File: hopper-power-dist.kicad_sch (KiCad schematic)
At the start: 30 parts, among them J1 XT90PW-M, J2 B2B-XH-A(LF)(SN), J3 XT60PW-F, J4 XT60PW-F, J5 XT60PW-F, J6 XT60PW-F, J7 XT60PW-F, J8 B2B-XH-A(LF)(SN), SW2 FT_Power_Switch

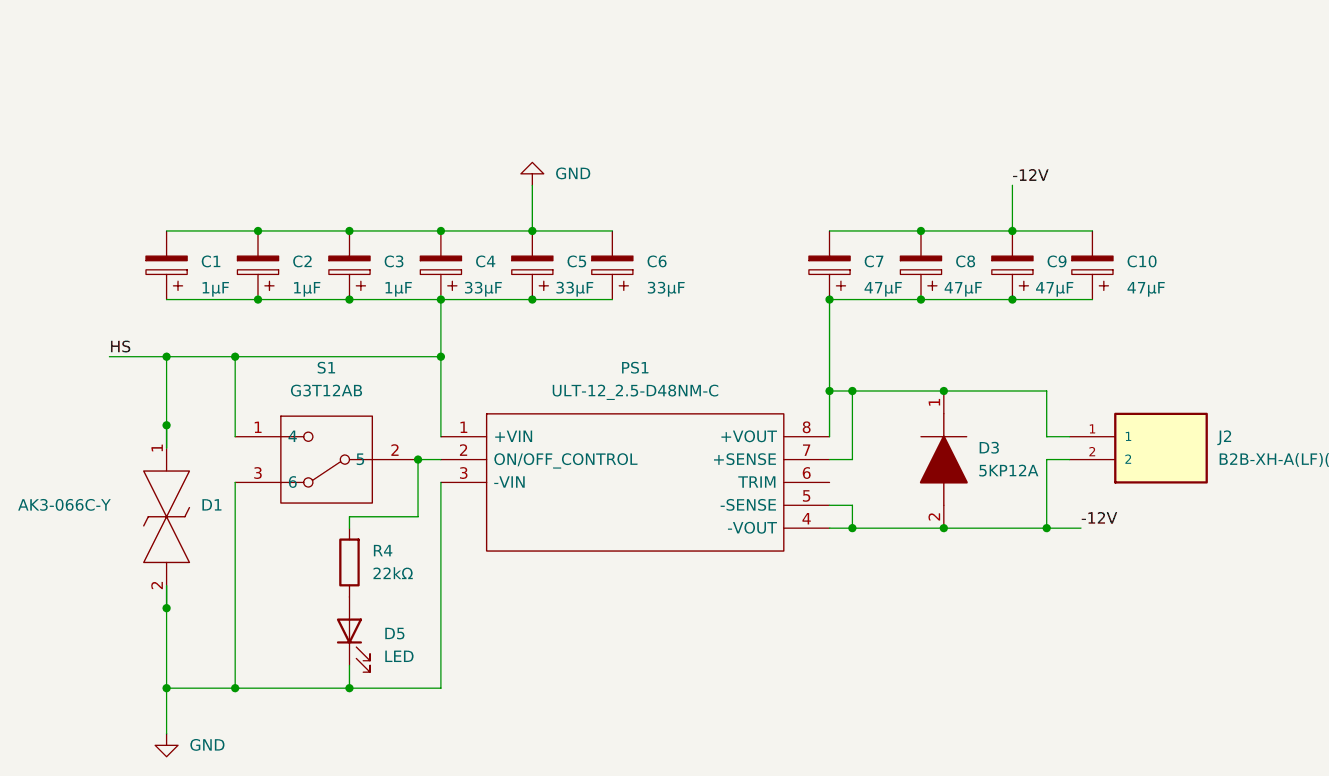
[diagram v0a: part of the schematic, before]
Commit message: Fix schematic and update 3d models
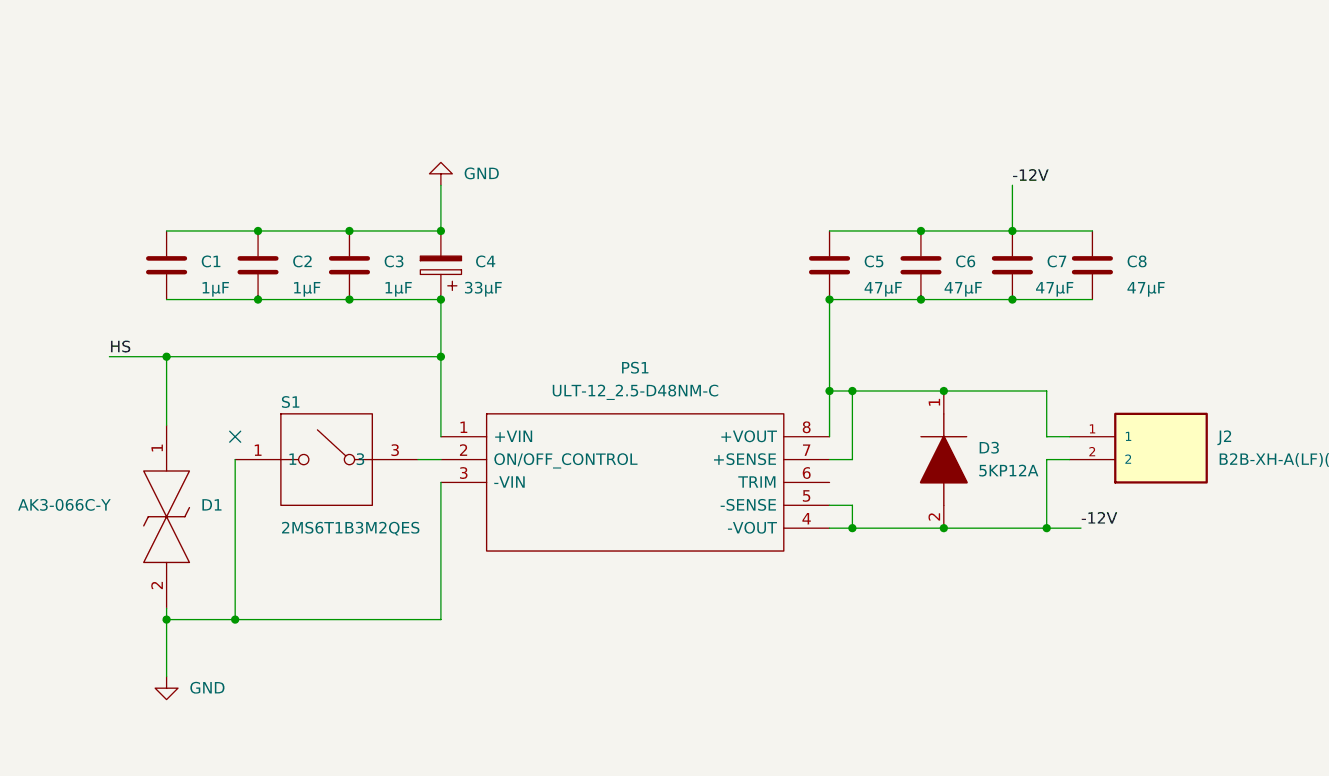
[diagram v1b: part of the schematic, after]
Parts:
- removed C5, C6: 33μF, Capacitor_SMD:CP_Elec_8x10, symbol Device:C_Polarized
- removed D5: LED, LED_SMD:LED_0603_1608Metric, symbol Device:LED
- removed R4: 22kΩ, Resistor_SMD:R_0603_1608Metric_Pad0.98x0.95mm_HandSolder, symbol Device:R
- removed S1: G3T12AB, G3T12AB, symbol SamacSys_Parts:G3T12AB
- added S1: 2MS6T1B3M2QES, 2MS6T1B3M2QES, symbol benbokser:2MS6T1B3M2QES
- C1, C2, C3: footprint Capacitor_SMD:CP_Elec_8x10 -> Capacitor_SMD:C_1206_3216Metric; symbol Device:C_Polarized -> Device:C
- C5: renamed from C7; footprint Capacitor_SMD:CP_Elec_8x10 -> Capacitor_SMD:C_2220_5650Metric; symbol Device:C_Polarized -> Device:C
- C6: renamed from C8; footprint Capacitor_SMD:CP_Elec_8x10 -> Capacitor_SMD:C_2220_5650Metric; symbol Device:C_Polarized -> Device:C
- C7: renamed from C9; footprint Capacitor_SMD:CP_Elec_8x10 -> Capacitor_SMD:C_2220_5650Metric; symbol Device:C_Polarized -> Device:C
- C8: renamed from C10; footprint Capacitor_SMD:CP_Elec_8x10 -> Capacitor_SMD:C_2220_5650Metric; symbol Device:C_Polarized -> Device:C
- R2: footprint SamacSys_Parts:RESAD5390W86L2222D792 -> benbokser:CW005900R0JB12
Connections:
- net GND: now also S1.1
- net at PS1.2 (ON/OFF_CONTROL): now also S1.3
- no-connect marks 0 -> 1

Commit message: Changed precharge resistor, routed PCB traces and updated 3D models
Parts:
- D3: footprint SamacSys_Parts:DIOAD4425W136L885D885 -> benbokser:5KP12A
- R2: value 900Ω -> 365Ω; footprint benbokser:CW005900R0JB12 -> benbokser:AC03000003600JAC00
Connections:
- no-connect marks 1 -> 0
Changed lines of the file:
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@@
   (junction (at 69.85 119.38) (diameter 0) (color 0 0 0 0)
   )
-  (no_connect (at 46.99 134.62))
   (wire (pts (xy 133.35 106.68) (xy 133.35 111.76))
     (stroke (width 0) (type default) (color 0 0 0 0))
@@
       (effects (font (size 1.27 1.27)) (justify left))
     )
-    (property "Footprint" "SamacSys_Parts:DIOAD4425W136L885D885" (id 2) (at 125.73 140.97 0)
+    (property "Footprint" "benbokser:5KP12A" (id 2) (at 125.73 140.97 0)
       (effects (font (size 1.27 1.27)) (justify left) hide)
     )
@@
     (in_bom yes) (on_board yes) (fields_autoplaced)
     (property "Reference" "R2" (id 0) (at 84.455 50.8 90))
-    (property "Value" "900Ω" (id 1) (at 84.455 53.34 90))
-    (property "Footprint" "benbokser:CW005900R0JB12" (id 2) (at 84.455 58.928 90)
+    (property "Value" "365Ω" (id 1) (at 84.455 53.34 90))
+    (property "Footprint" "benbokser:AC03000003600JAC00" (id 2) (at 84.455 58.928 90)
       (effects (font (size 1.27 1.27)) hide)
     )
@@
     )
     (path "/6d558682-e19a-4c65-b77e-d608f0f3e1f5"
-      (reference "D3") (unit 1) (value "5KP12A") (footprint "SamacSys_Parts:DIOAD4425W136L885D885")
+      (reference "D3") (unit 1) (value "5KP12A") (footprint "benbokser:5KP12A")
     )
     (path "/612105e5-ac66-49d2-a8fd-540e901763e8"
@@
     )
     (path "/c5098257-5571-47c3-a82b-49312500a93f"
-      (reference "R2") (unit 1) (value "900Ω") (footprint "benbokser:CW005900R0JB12")
+      (reference "R2") (unit 1) (value "365Ω") (footprint "benbokser:AC03000003600JAC00")
     )
     (path "/d9f35c5b-7a24-4156-809c-cf432f477e68"

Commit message: Start rev02, fix minor mistakes and add xt60pw-m series
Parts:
- removed D2: LED, LED_SMD:LED_0603_1608Metric, symbol Device:LED
- removed J1: XT90PW-M, XT90PW-M:AMASS_XT90PW-M, symbol XT90PW-M:XT90PW-M
- removed R1: 22kΩ, Resistor_SMD:R_0603_1608Metric_Pad0.98x0.95mm_HandSolder, symbol Device:R
- added H1: B-, MountingHole:MountingHole_4.3mm_M4_Pad_Via, symbol Mechanical:MountingHole_Pad
- added H2: C-, MountingHole:MountingHole_4.3mm_M4_Pad_Via, symbol Mechanical:MountingHole_Pad
- added J1, J2: XT60PW-M, XT60PW-F:AMASS_XT60PW-M, symbol XT60PW-F:XT60PW-M
- C4: footprint Capacitor_SMD:CP_Elec_8x10 -> benbokser:CP_Elec_8x10_MAL214699903E3
- D1: footprint SamacSys_Parts:AK3066CY -> AK3066CY
- J3: renamed from J8; footprint B2B-XH-A_LF__SN_:JST_B2B-XH-A(LF)(SN) -> JST_B2B-XH-A(LF)(SN)
- J4: renamed from J2; footprint B2B-XH-A_LF__SN_:JST_B2B-XH-A(LF)(SN) -> JST_B2B-XH-A(LF)(SN)
- J5: renamed from J3; footprint XT60PW-F:AMASS_XT60PW-F -> AMASS_XT60PW-F
- J6: renamed from J4; footprint XT60PW-F:AMASS_XT60PW-F -> AMASS_XT60PW-F
- J7: renamed from J5; footprint XT60PW-F:AMASS_XT60PW-F -> AMASS_XT60PW-F
- J8: renamed from J6; footprint XT60PW-F:AMASS_XT60PW-F -> AMASS_XT60PW-F
- J9: renamed from J7; footprint XT60PW-F:AMASS_XT60PW-F -> AMASS_XT60PW-F
- PS1: footprint SamacSys_Parts:ULT1225D48NMC -> ULT1225D48NMC
- renumbered D3 to D2, D4 to D3, R2 to R1, R3 to R2, SW2 to SW1
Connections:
- net GND: now also H2.1; no longer J5.S1 (SHIELD), J5.S2 (SHIELD), J6.S1 (SHIELD), J6.S2 (SHIELD), J7.S1 (SHIELD), J7.S2 (SHIELD), J8.S1 (SHIELD), J8.S2 (SHIELD), J9.S1 (SHIELD), J9.S2 (SHIELD)
- net at J3.2, SW1.1: now also J2.1 (+)
- new net: J1.1 (+), J2.2 (-)
- new net: H1.1, J1.2 (-)
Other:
- moved on the sheet: J3, R1, SW1

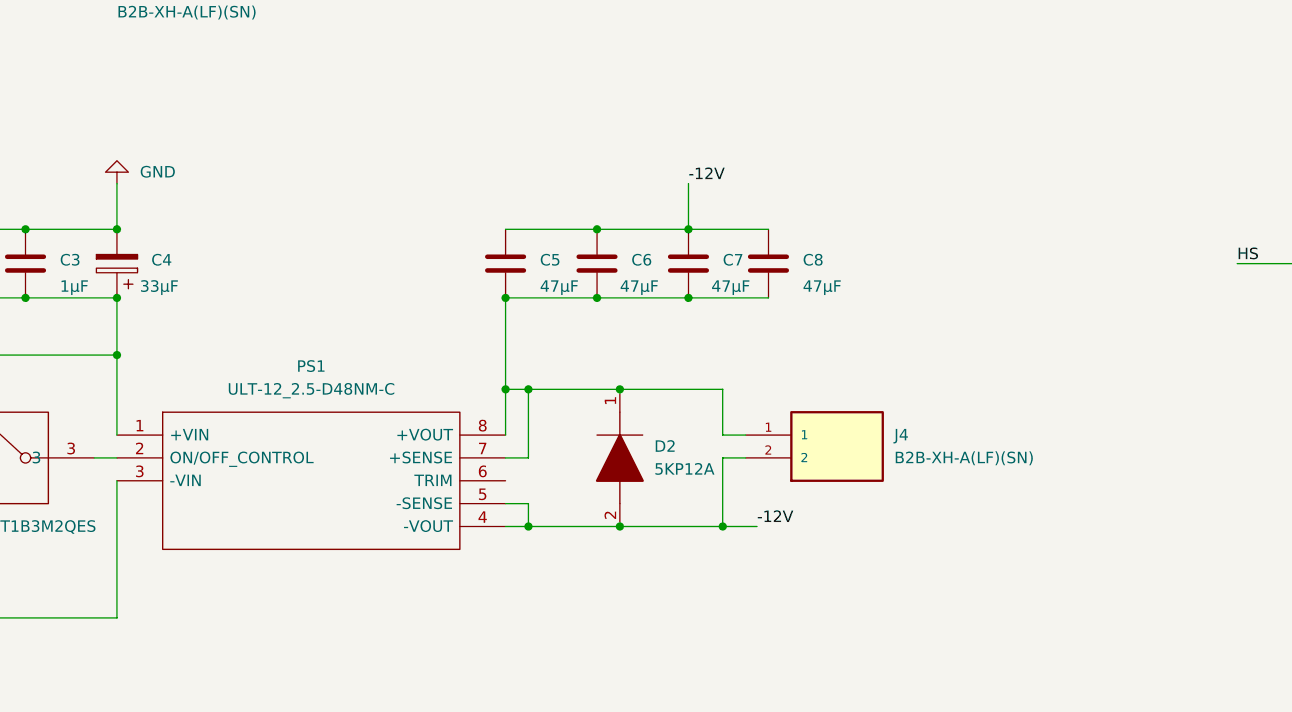
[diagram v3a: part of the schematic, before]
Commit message: Replace DC-DC converter with thru-hole version and clean up
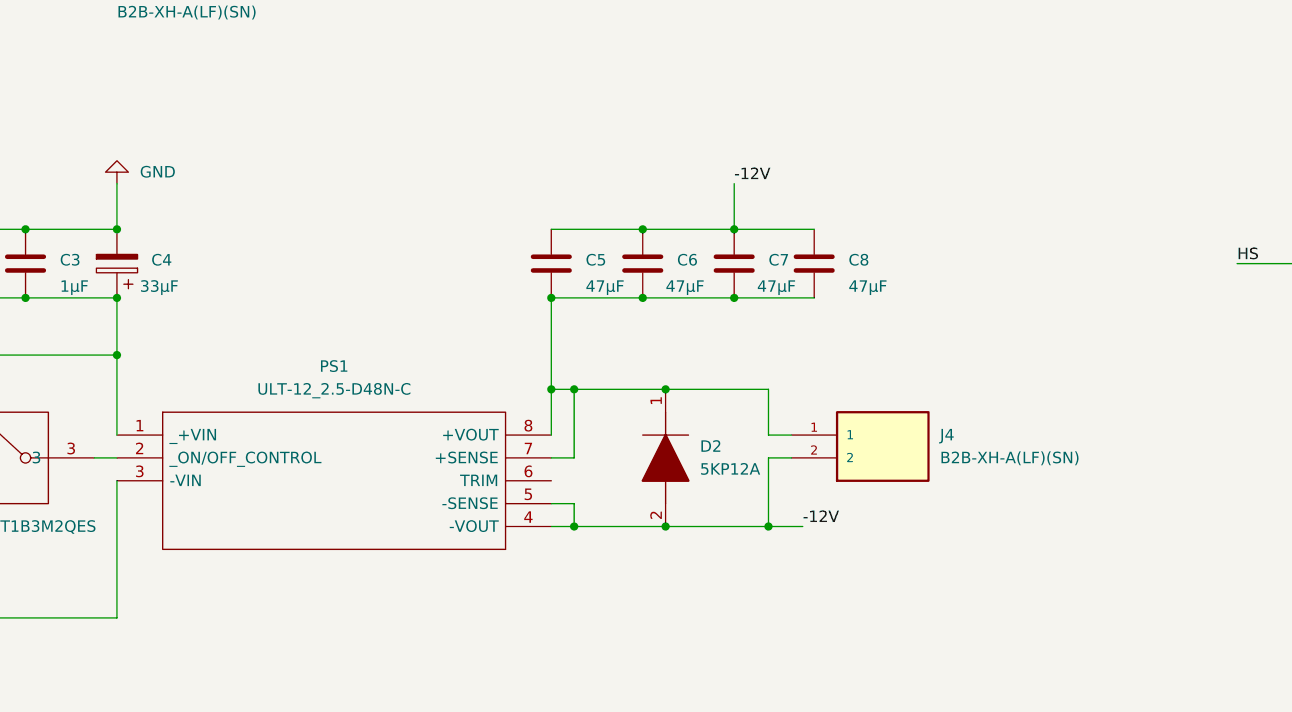
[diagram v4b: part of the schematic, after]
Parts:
- PS1: value ULT-12_2.5-D48NM-C -> ULT-12_2.5-D48N-C; footprint ULT1225D48NMC -> SamacSys_Parts:ULT1225D48NC; symbol SamacSys_Parts:ULT-12_2.5-D48NM-C -> SamacSys_Parts:ULT-12_2.5-D48N-C; Height 9.398 -> 8.9; Manufacturer_Part_Number ULT-12/2.5-D48NM-C -> ULT-12/2.5-D48N-C; Mouser Part Number 580-ULT-12/2.5D48NMC -> 580-ULT-12/2.5-D48NC; Mouser Price/Stock https://www.mouser.co.uk/ProductDetail/Murata-Power-Solutions/ULT-12-25-D48NM-C?qs=pygdPweA0RfIXL%2FkWB89cA%3D%3D -> https://www.mouser.co.uk/ProductDetail/Murata-Power-Solutions/ULT-12-25-D48N-C?qs=pygdPweA0RfWvar2Gkh2JA%3D%3D
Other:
- moved on the sheet: C5, C6, C7, C8, D2, J4, PS1

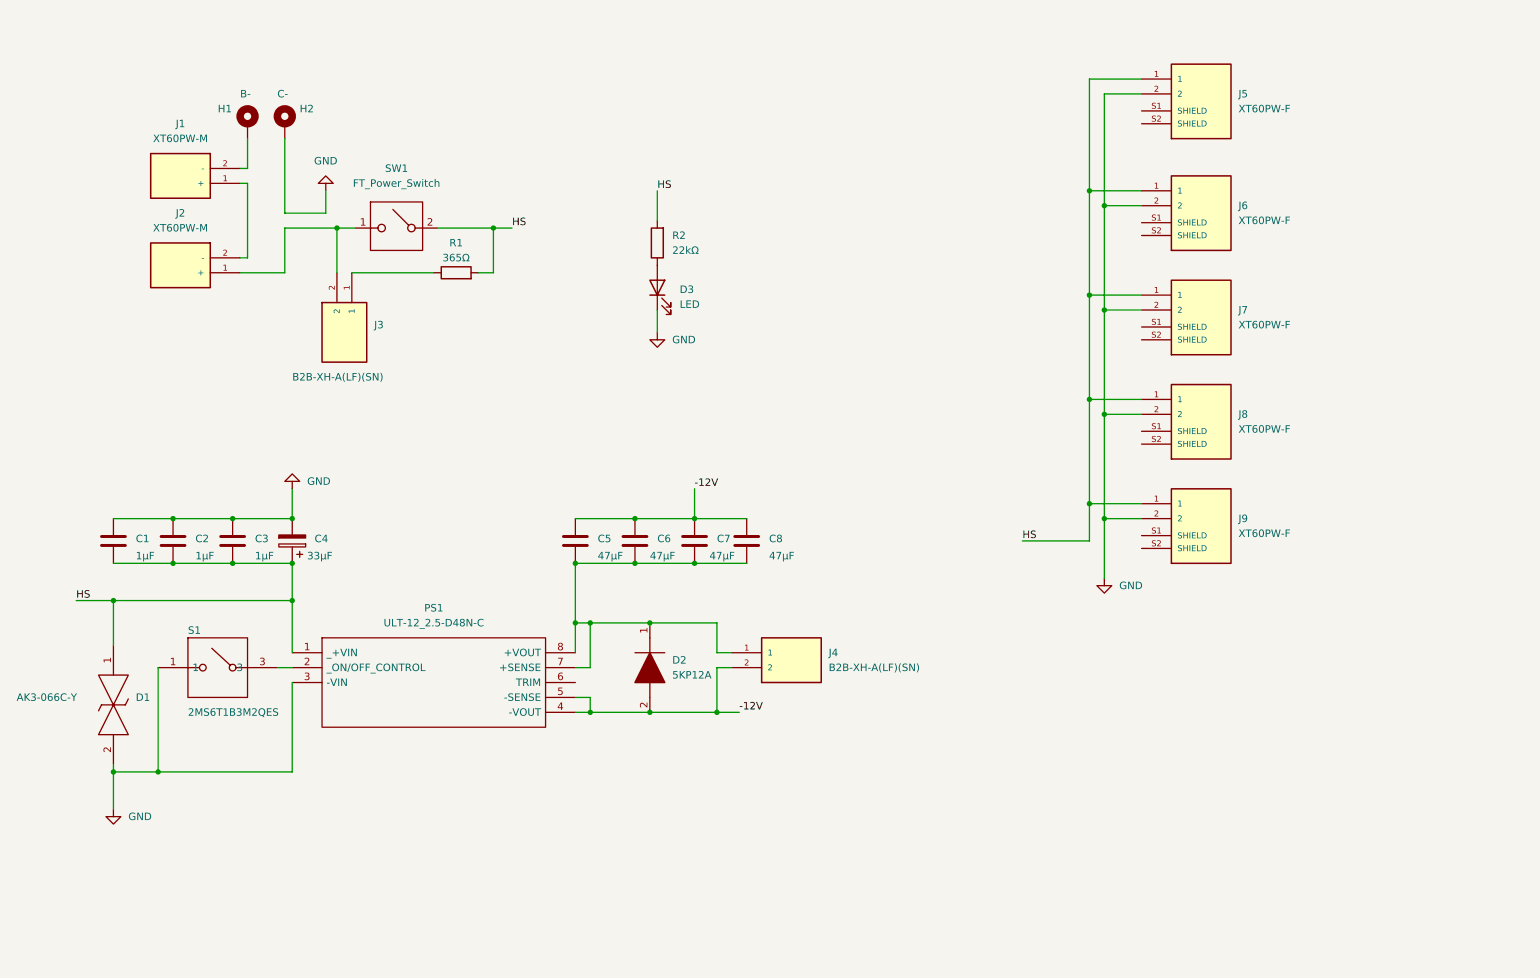
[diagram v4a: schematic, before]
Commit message: Replaced DC-DC Converter and working on capacitor selection
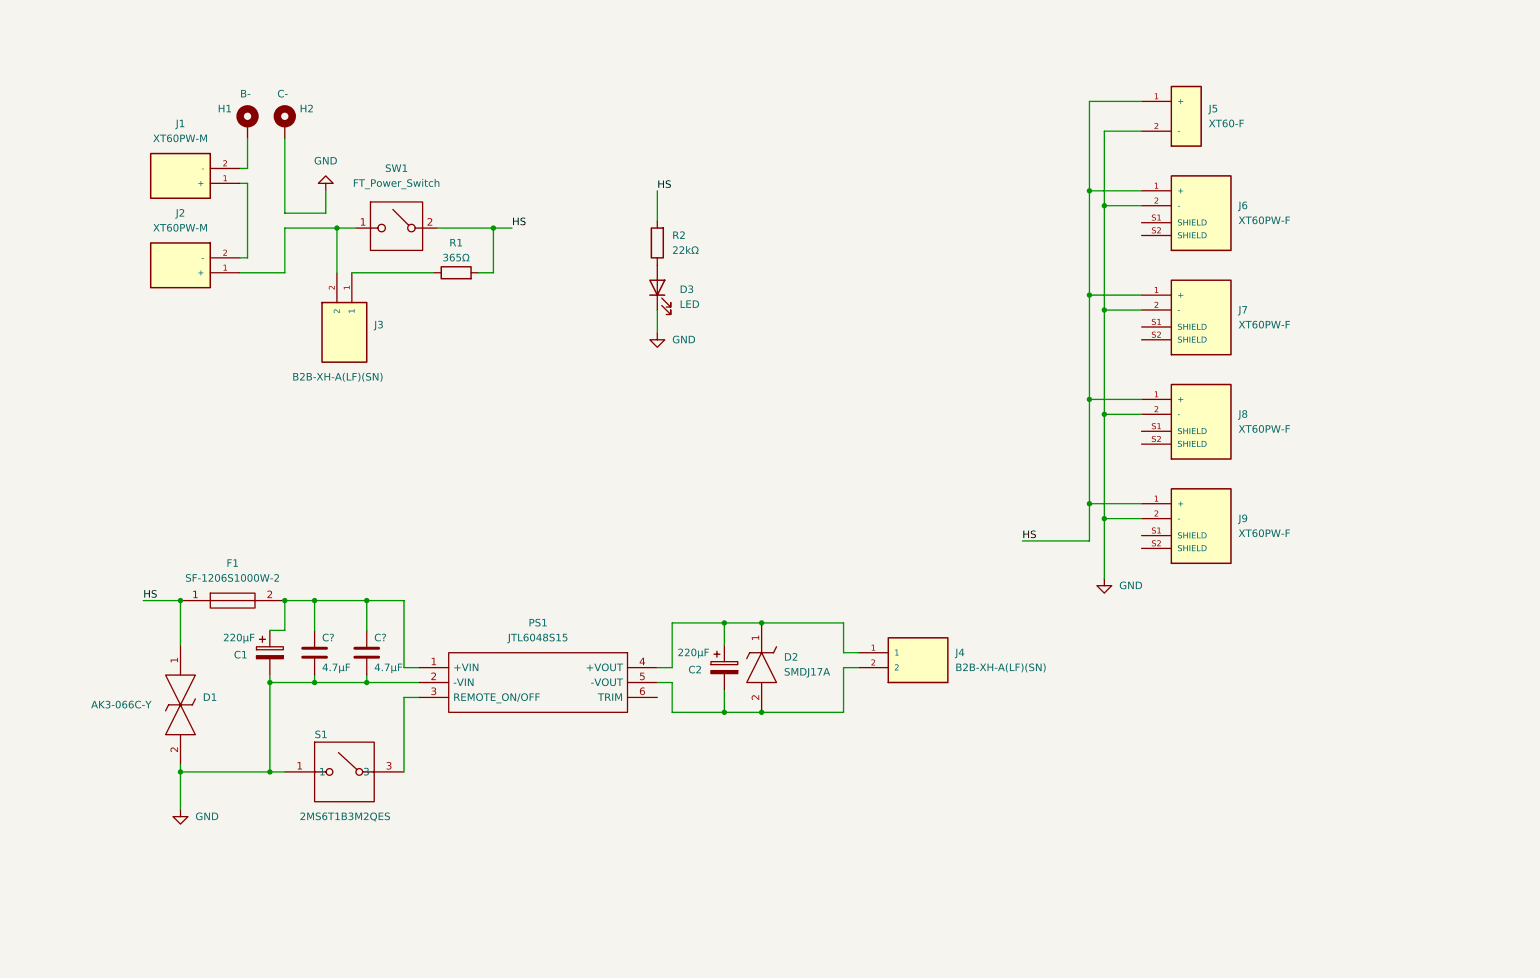
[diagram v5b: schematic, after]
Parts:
- removed C1, C2, C3: 1μF, Capacitor_SMD:C_1206_3216Metric, symbol Device:C
- removed C4: 33μF, benbokser:CP_Elec_8x10_MAL214699903E3, symbol Device:C_Polarized
- removed C5, C6, C7, C8: 47μF, Capacitor_SMD:C_2220_5650Metric, symbol Device:C
- removed D2: 5KP12A, benbokser:5KP12A, symbol SamacSys_Parts:5KP12A
- removed J5: XT60PW-F, AMASS_XT60PW-F, symbol XT60PW-F:XT60PW-F
- added C1, C2: 220μF, benbokser:CP_Elec_8x10_150CRZ, symbol Device:C_Polarized
- added C?: 4.7μF, SamacSys_Parts:CAPC3225X270N, symbol Device:C
- added C?: 4.7μF, symbol Device:C
- added D2: SMDJ17A, DIOM7959X262N, symbol SamacSys_Parts:SMDJ17A
- added F1: SF-1206S1000W-2, FUSC3216X123N, symbol SamacSys_Parts:SF-1206S1000W-2
- added J5: XT60-F, XT60PW-F:AMASS_XT60-F, symbol XT60PW-F:XT60-F
- D1: footprint AK3066CY -> SamacSys_Parts:AK3066CY
- PS1: value ULT-12_2.5-D48N-C -> JTL6048S15; footprint SamacSys_Parts:ULT1225D48NC -> JTL6048S15; symbol SamacSys_Parts:ULT-12_2.5-D48N-C -> SamacSys_Parts:JTL6048S15; Height 8.9 -> 12; Manufacturer_Name Murata Electronics -> XP POWER; Manufacturer_Part_Number ULT-12/2.5-D48N-C -> JTL6048S15; Mouser Part Number 580-ULT-12/2.5-D48NC -> 209-JTL6048S15; Mouser Price/Stock https://www.mouser.co.uk/ProductDetail/Murata-Power-Solutio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 -> https://www.mouser.co.uk/ProductDetail/XP-Power/JTL6048S15?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
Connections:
- net GND: now also PS1.2 (-VIN), C1.2, C?.2, C?.2, J5.2 (-); no longer PS1.3 (-VIN)
- net HS: now also F1.1, J5.1 (+); no longer PS1.1 (_+VIN)
- net at S1.3: now also PS1.3 (REMOTE_ON/OFF); no longer PS1.2 (_ON/OFF_CONTROL)
- net -12V: no longer names the net of J4.2, PS1.5 (-VOUT)
- net -12V: now also C2.2, D2.2; no longer PS1.4 (-VOUT)
- new net: C1.1, C?.1, C?.1, F1.2, PS1.1 (+VIN)
- new net: C2.1, D2.1, J4.1, PS1.4 (+VOUT)
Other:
- moved on the sheet: D1, J4, S1

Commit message: Further tweaks to v2 design
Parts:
- removed C1, C2: 220μF, benbokser:CP_Elec_8x10_150CRZ, symbol Device:C_Polarized
- added C4, C5: 1000pF, Capacitor_SMD:C_1206_3216Metric, symbol Device:C
- added C6: 470pF, Capacitor_SMD:C_1206_3216Metric, symbol Device:C
- added L1, L2: 12μF, SamacSys_Parts:LPS6235123MRC, symbol Device:L
- C3: renamed from C?; footprint (none) -> Capacitor_SMD:C_0805_2012Metric
- R1: value 365Ω -> 360Ω
- gave numbers to parts that had none: 1
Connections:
- net GND: now also C5.1, L2.1; no longer C3.2, PS1.2 (-VIN)
- net at C2.1, F1.2: now also L1.1; no longer C3.1, PS1.1 (+VIN)
- net +12V: now reaches D2.1, J4.1, PS1.4 (+VOUT)
- net +12V: now also C4.2
- net -12V: now reaches D2.2, J4.2, PS1.5 (-VOUT)
- net -12V: now also C5.2, C6.2
- new net: C3.2, L2.2, PS1.2 (-VIN)
- new net: C3.1, C4.1, C6.1, L1.2, PS1.1 (+VIN)
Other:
- moved on the sheet: C2, C3, D1, D2, F1, J4, S1
